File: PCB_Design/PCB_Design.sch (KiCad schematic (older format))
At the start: 19 parts, among them SW1 SW_Push, SW2 SW_Push, U1 ESP32-WROOM-32

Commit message: PCB organizada con casi todo SMD
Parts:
- Conn_I2C1: footprint Connector_PinSocket_2.54mm:PinSocket_1x03_P2.54mm_Horizontal -> Connector_PinSocket_2.54mm:PinSocket_1x03_P2.54mm_Vertical_SMD_Pin1Left
- Conn_OLED1: footprint Connector_PinSocket_2.54mm:PinSocket_1x04_P2.54mm_Vertical -> Connector_PinSocket_2.54mm:PinSocket_1x04_P2.54mm_Vertical_SMD_Pin1Left
- Conn_prog1: footprint Connector_PinSocket_2.54mm:PinSocket_1x05_P2.54mm_Horizontal -> Connector_PinSocket_2.54mm:PinSocket_1x05_P2.54mm_Vertical_SMD_Pin1Left
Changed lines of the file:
@@
 F 0 "Conn_OLED1" H 5233 3281 50  0000 L CNN
 F 1 "Conn_01x04_Female" H 5233 3190 50  0000 L CNN
-F 2 "Connector_PinSocket_2.54mm:PinSocket_1x04_P2.54mm_Vertical" H 5205 3305 50  0001 C CNN
+F 2 "Connector_PinSocket_2.54mm:PinSocket_1x04_P2.54mm_Vertical_SMD_Pin1Left" H 5205 3305 50  0001 C CNN
 F 3 "~" H 5205 3305 50  0001 C CNN
 	1    5205 3305
@@
 F 0 "Conn_I2C1" H 5233 3881 50  0000 L CNN
 F 1 "Conn_01x03_Female" H 5233 3790 50  0000 L CNN
-F 2 "Connector_PinSocket_2.54mm:PinSocket_1x03_P2.54mm_Horizontal" H 5205 3855 50  0001 C CNN
+F 2 "Connector_PinSocket_2.54mm:PinSocket_1x03_P2.54mm_Vertical_SMD_Pin1Left" H 5205 3855 50  0001 C CNN
 F 3 "~" H 5205 3855 50  0001 C CNN
 	1    5205 3855
@@
 F 0 "Conn_prog1" H 4873 1931 50  0000 L CNN
 F 1 "Conn_01x05_Female" H 4873 1840 50  0000 L CNN
-F 2 "Connector_PinSocket_2.54mm:PinSocket_1x05_P2.54mm_Horizontal" H 4845 1905 50  0001 C CNN
+F 2 "Connector_PinSocket_2.54mm:PinSocket_1x05_P2.54mm_Vertical_SMD_Pin1Left" H 4845 1905 50  0001 C CNN
 F 3 "~" H 4845 1905 50  0001 C CNN
 	1    4845 1905

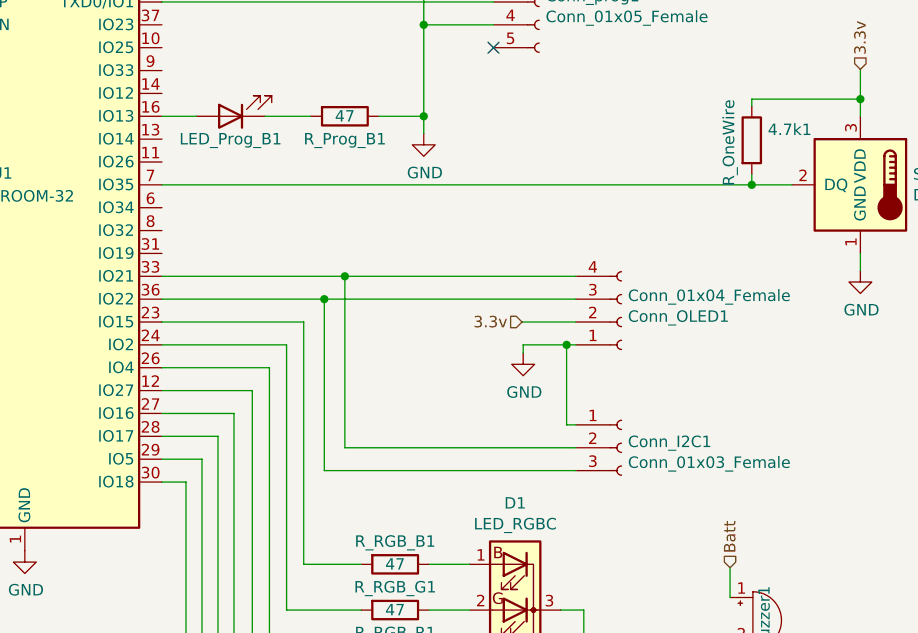
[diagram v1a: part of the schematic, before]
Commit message: Caminos de la PCB sin GND
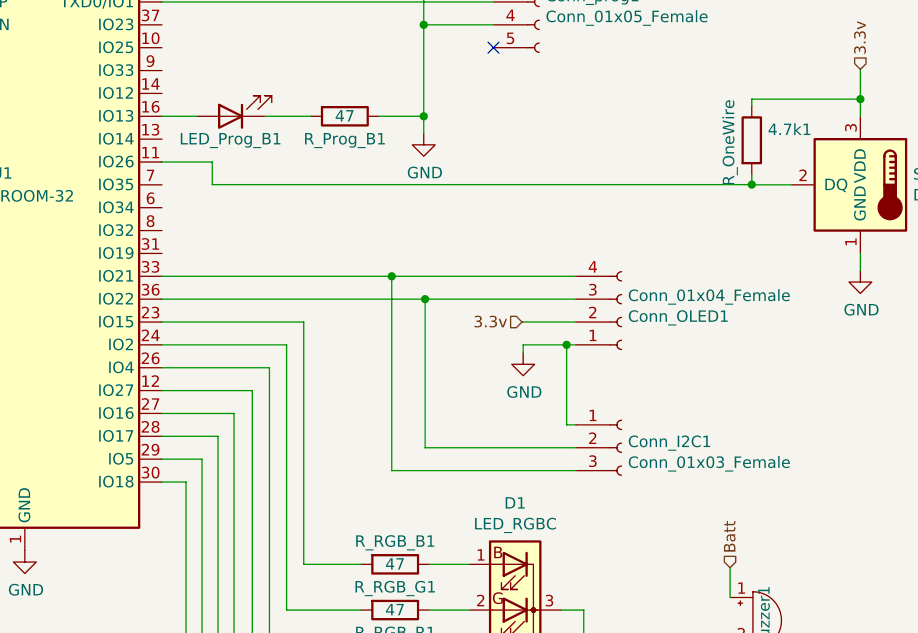
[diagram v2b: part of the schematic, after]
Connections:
- net at U1.11 (IO26): now also 4.7k1.2, Sens_Temp1.2 (DQ)
- net at Conn_OLED1.4 (Pin_4), U1.33 (IO21): now also Conn_I2C1.3 (Pin_3); no longer Conn_I2C1.2 (Pin_2)
- net at Conn_OLED1.3 (Pin_3), U1.36 (IO22): now also Conn_I2C1.2 (Pin_2); no longer Conn_I2C1.3 (Pin_3)
- now unconnected: U1.7 (IO35)
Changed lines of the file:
@@
 	3815 3305 3815 4365
-Wire Wire Line
-	3195 3105 3995 3105
-Wire Wire Line
-	5005 3205 3905 3205
 Wire Wire Line
 	4770 3305 5005 3305
 Wire Wire Line
 	4775 3440 4775 3405
-Wire Wire Line
-	5005 3955 3905 3955
-Wire Wire Line
-	3905 3955 3905 3205
-Connection ~ 3905 3205
-Wire Wire Line
-	3905 3205 3195 3205
-Wire Wire Line
-	5005 3855 3995 3855
-Wire Wire Line
-	3995 3855 3995 3105
-Connection ~ 3995 3105
-Wire Wire Line
-	3995 3105 5005 3105
 Wire Wire Line
 	5005 3755 4965 3755
@@
 	5950 2705 5775 2705
 Wire Wire Line
-	5775 2705 5775 2660
+	5775 2705 5775 2704
 Wire Wire Line
 	5775 2360 5775 2330
@@
 Wire Wire Line
 	6250 2330 6250 2405
-Wire Wire Line
-	5775 2705 3195 2705
-Connection ~ 5775 2705
 NoConn ~ 4645 2105
 Wire Wire Line
@@
 	1    0    0    -1
 $EndComp
+Wire Wire Line
+	3195 3205 4346 3205
+Wire Wire Line
+	3195 3105 4200 3105
+Wire Wire Line
+	5005 3855 4346 3855
+Wire Wire Line
+	4346 3855 4346 3205
+Connection ~ 4346 3205
+Wire Wire Line
+	4346 3205 5005 3205
+Wire Wire Line
+	4200 3105 4200 3955
+Wire Wire Line
+	4200 3955 5005 3955
+Connection ~ 4200 3105
+Wire Wire Line
+	4200 3105 5005 3105
+Wire Wire Line
+	3195 2605 3415 2605
+Wire Wire Line
+	3415 2605 3415 2704
+Wire Wire Line
+	3415 2704 5775 2704
+Connection ~ 5775 2704
+Wire Wire Line
+	5775 2704 5775 2660
 $EndSCHEMATC

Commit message: PCB diseño fianl retocado + lista componentes
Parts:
- removed Conn_I2C1: Conn_01x03_Female, Connector_PinSocket_2.54mm:PinSocket_1x03_P2.54mm_Vertical_SMD_Pin1Left, symbol Connector:Conn_01x03_Female
- added C_bypass1: 100pF, Capacitor_SMD:C_0805_2012Metric_Pad1.18x1.45mm_HandSolder, symbol Device:C
- added Conn_I2C1: Conn_01x04_Female, Connector_PinSocket_2.54mm:PinSocket_1x04_P2.54mm_Vertical_SMD_Pin1Left, symbol Connector:Conn_01x04_Female
- D1: symbol Device:LED_RGBC -> PCB_Design-rescue:LED_RGBC-Device
- SW1, SW2: footprint Button_Switch_SMD:SW_SPST_B3U-1000P -> Button_Switch_SMD:SW_SPST_CK_RS282G05A3
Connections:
- wire segments 96 -> 103
- no-connect marks 1 -> 17
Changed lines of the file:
@@
 F 0 "SW1" H 1445 1855 50  0000 C CNN
 F 1 "SW_Push" H 1445 1655 50  0000 C CNN
-F 2 "Button_Switch_SMD:SW_SPST_B3U-1000P" H 1445 1905 50  0001 C CNN
+F 2 "Button_Switch_SMD:SW_SPST_CK_RS282G05A3" H 1445 1905 50  0001 C CNN
 F 3 "~" H 1445 1905 50  0001 C CNN
 	1    1445 1705
@@
 F 0 "SW2" H 3795 1855 50  0000 C CNN
 F 1 "SW_Push" H 3795 1655 50  0000 C CNN
-F 2 "Button_Switch_SMD:SW_SPST_B3U-1000P" H 3795 1905 50  0001 C CNN
+F 2 "Button_Switch_SMD:SW_SPST_CK_RS282G05A3" H 3795 1905 50  0001 C CNN
 F 3 "~" H 3795 1905 50  0001 C CNN
 	1    3795 1705
@@
 $EndComp
 $Comp
-L Connector:Conn_01x03_Female Conn_I2C1
-U 1 1 61B269DE
-P 5205 3855
-F 0 "Conn_I2C1" H 5233 3881 50  0000 L CNN
-F 1 "Conn_01x03_Female" H 5233 3790 50  0000 L CNN
-F 2 "Connector_PinSocket_2.54mm:PinSocket_1x03_P2.54mm_Vertical_SMD_Pin1Left" H 5205 3855 50  0001 C CNN
-F 3 "~" H 5205 3855 50  0001 C CNN
-	1    5205 3855
-	1    0    0    -1
-$EndComp
-$Comp
 L power:GND #PWR0104
 U 1 1 61B29741
@@
 	7480 1840 7480 1945
 $Comp
-L Device:LED_RGBC D1
+L PCB_Design-rescue:LED_RGBC-Device D1
 U 1 1 61B93938
 P 4740 4565
@@
 	3815 3305 3815 4365
 Wire Wire Line
-	4770 3305 5005 3305
+	4770 3305 5000 3305
 Wire Wire Line
 	4775 3440 4775 3405
 Wire Wire Line
-	5005 3755 4965 3755
+	5005 3755 5000 3755
 Wire Wire Line
 	4965 3755 4965 3405
@@
 	3195 3105 4200 3105
 Wire Wire Line
-	5005 3855 4346 3855
+	5005 3855 5000 3855
 Wire Wire Line
 	4346 3855 4346 3205
@@
 	4200 3105 4200 3955
 Wire Wire Line
-	4200 3955 5005 3955
+	4200 3955 5000 3955
 Connection ~ 4200 3105
 Wire Wire Line
@@
 Wire Wire Line
 	5775 2704 5775 2660
+NoConn ~ 1995 3405
+NoConn ~ 1995 3305
+NoConn ~ 1995 3205
+NoConn ~ 1995 3105
+NoConn ~ 1995 3005
+NoConn ~ 1995 2905
+NoConn ~ 1995 2005
+NoConn ~ 1995 1905
+NoConn ~ 3195 2005
+NoConn ~ 3195 2105
+NoConn ~ 3195 2205
+NoConn ~ 3195 2505
+NoConn ~ 3195 2705
+NoConn ~ 3195 2805
+NoConn ~ 3195 2905
+NoConn ~ 3195 3005
+$Comp
+L Device:C C_bypass1
+U 1 1 61BEC39E
+P 2985 1405
+F 0 "C_bypass1" V 2733 1405 50  0000 C CNN
+F 1 "100pF" V 2824 1405 50  0000 C CNN
+F 2 "Capacitor_SMD:C_0805_2012Metric_Pad1.18x1.45mm_HandSolder" H 3023 1255 50  0001 C CNN
+F 3 "~" H 2985 1405 50  0001 C CNN
+	1    2985 1405
+	0    1    1    0
+$EndComp
+$Comp
+L power:GND #PWR0126
+U 1 1 61BECE85
+P 3240 1405
+F 0 "#PWR0126" H 3240 1155 50  0001 C CNN
+F 1 "GND" H 3245 1232 50  0000 C CNN
+F 2 "" H 3240 1405 50  0001 C CNN
+F 3 "" H 3240 1405 50  0001 C CNN
+	1    3240 1405
+	0    -1   -1   0
+$EndComp
+Wire Wire Line
+	2835 1405 2595 1405
+Wire Wire Line
+	3240 1405 3135 1405
+$Comp
+L Connector:Conn_01x04_Female Conn_I2C1
+U 1 1 61C17C1F
+P 5200 3855
+F 0 "Conn_I2C1" H 5228 3831 50  0000 L CNN
+F 1 "Conn_01x04_Female" H 5228 3740 50  0000 L CNN
+F 2 "Connector_PinSocket_2.54mm:PinSocket_1x04_P2.54mm_Vertical_SMD_Pin1Left" H 5200 3855 50  0001 C CNN
+F 3 "~" H 5200 3855 50  0001 C CNN
+	1    5200 3855
+	1    0    0    1
+$EndComp
+Connection ~ 5000 3955
+Wire Wire Line
+	5000 3955 5005 3955
+Connection ~ 5000 3855
+Wire Wire Line
+	5000 3855 4346 3855
+Connection ~ 5000 3755
+Wire Wire Line
+	5000 3755 4965 3755
+Wire Wire Line
+	5000 3655 5000 3305
+Connection ~ 5000 3305
+Wire Wire Line
+	5000 3305 5005 3305
 $EndSCHEMATC
